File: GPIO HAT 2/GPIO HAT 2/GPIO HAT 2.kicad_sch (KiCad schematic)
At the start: 99 parts, among them J1 ., J10 ., J11 ., J12 ., J13 ., J14 ., J15 ., J16 ., J17 ., J18 ., J19 ., J2 ., J20 ., J21 LVDS, J22 LVDS, J23 02x02, J24 USB_C_Receptacle_PowerOnly_6P, J3 ., J4 ., J5 ., J6 ., J7 ., J8 ., J9 ., U1 TXB0108DQSR, U10 TXB0108DQSR, U12 SY8088IAAC, U13 SY8088IAAC, U14 TPS2117, U2 TXB0108DQSR, U3 TXB0108DQSR, U4 TXB0108DQSR, U5 TXB0108DQSR, U6 TXB0108DQSR, U7 TXB0108DQSR, U8 TXB0108DQSR, U9 TXB0108DQSR

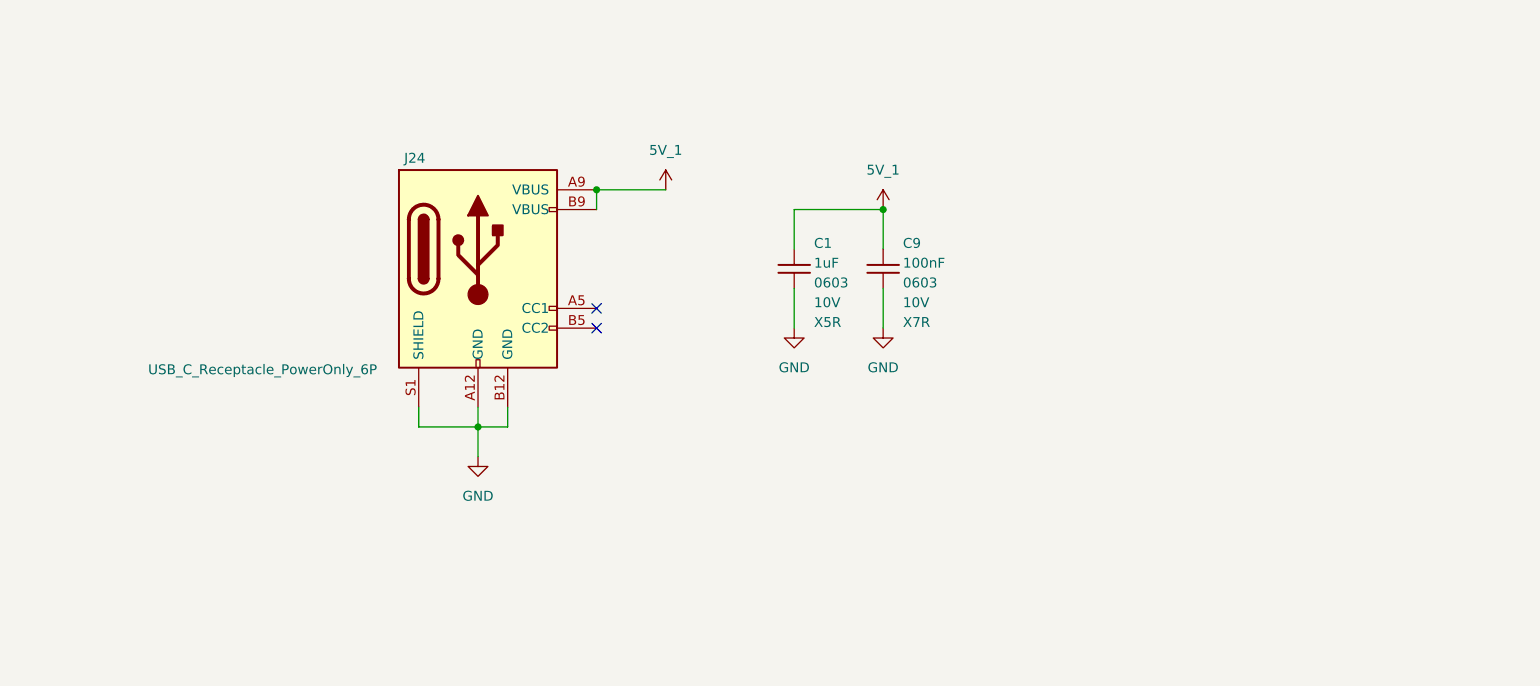
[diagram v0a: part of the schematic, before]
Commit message: 12V Jack removed and 5V USB added
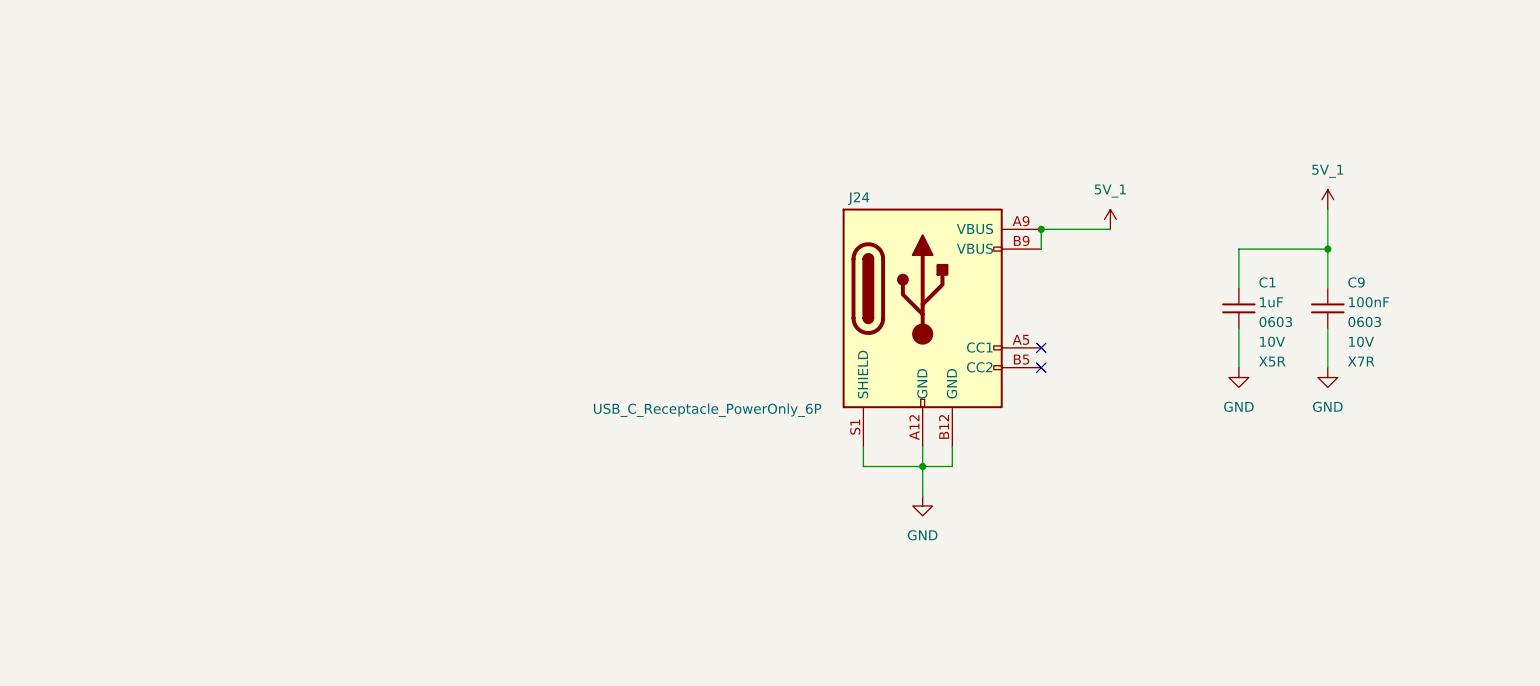
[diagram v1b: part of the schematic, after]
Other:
- moved on the sheet: C1, C9, J24
